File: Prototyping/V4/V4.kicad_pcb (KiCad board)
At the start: 2 copper layers, 126.7 x 100.2 mm, 117 parts, among them J1 Conn_02x04_Odd_Even, SW1 SW_Push_45deg, SW10 SW_Push_45deg, SW11 SW_Push_45deg, SW12 SW_Push_45deg, SW13 SW_Push_45deg, SW14 SW_Push_45deg, SW15 SW_Push_45deg, SW16 SW_Push_45deg, SW17 SW_Push_45deg, SW18 SW_Push_45deg, SW19 SW_Push_45deg, SW2 SW_Push_45deg, SW20 SW_Push_45deg, SW21 SW_Push_45deg, SW22 SW_Push_45deg, SW23 SW_Push_45deg, SW24 SW_Push_45deg, SW25 SW_Push_45deg, SW26 SW_Push_45deg, SW27 SW_Push_45deg, SW28 SW_Push_45deg, SW29 SW_Push_45deg, SW3 SW_Push_45deg, SW30 SW_Push_45deg, SW31 SW_Push_45deg, SW32 SW_Push_45deg, SW33 SW_Push_45deg, SW34 SW_Push_45deg, SW35 SW_Push_45deg, SW36 SW_Push_45deg, SW37 SW_Push_45deg, SW38 SW_Push_45deg, SW39 SW_Push_45deg, SW4 SW_Push_45deg, SW40 SW_Push_45deg, SW41 SW_Push_45deg, SW42 SW_Push_45deg, SW43 SW_Push_45deg, SW44 SW_Push_45deg, SW45 SW_Push_45deg, SW46 SW_Push_45deg, SW47 SW_Push_45deg, SW48 SW_Push_45deg, SW5 SW_Push_45deg, SW51 SW_Push_45deg, SW52 SW_Push_45deg, SW53 SW_Push_45deg, SW54 SW_Push_45deg, SW55 SW_Push_45deg, SW56 SW_Push_45deg, SW57 SW_Push_45deg, SW58 SW_Push_45deg, SW6 SW_Push_45deg, SW7 SW_Push_45deg, SW8 SW_Push_45deg, SW9 SW_Push_45deg

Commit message: validating
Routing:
- net Row 2: track 141.4 -> 144.8 mm
- net Row 1: track 121.1 -> 121.8 mm
- net C56: track 306.2 -> 306.8 mm

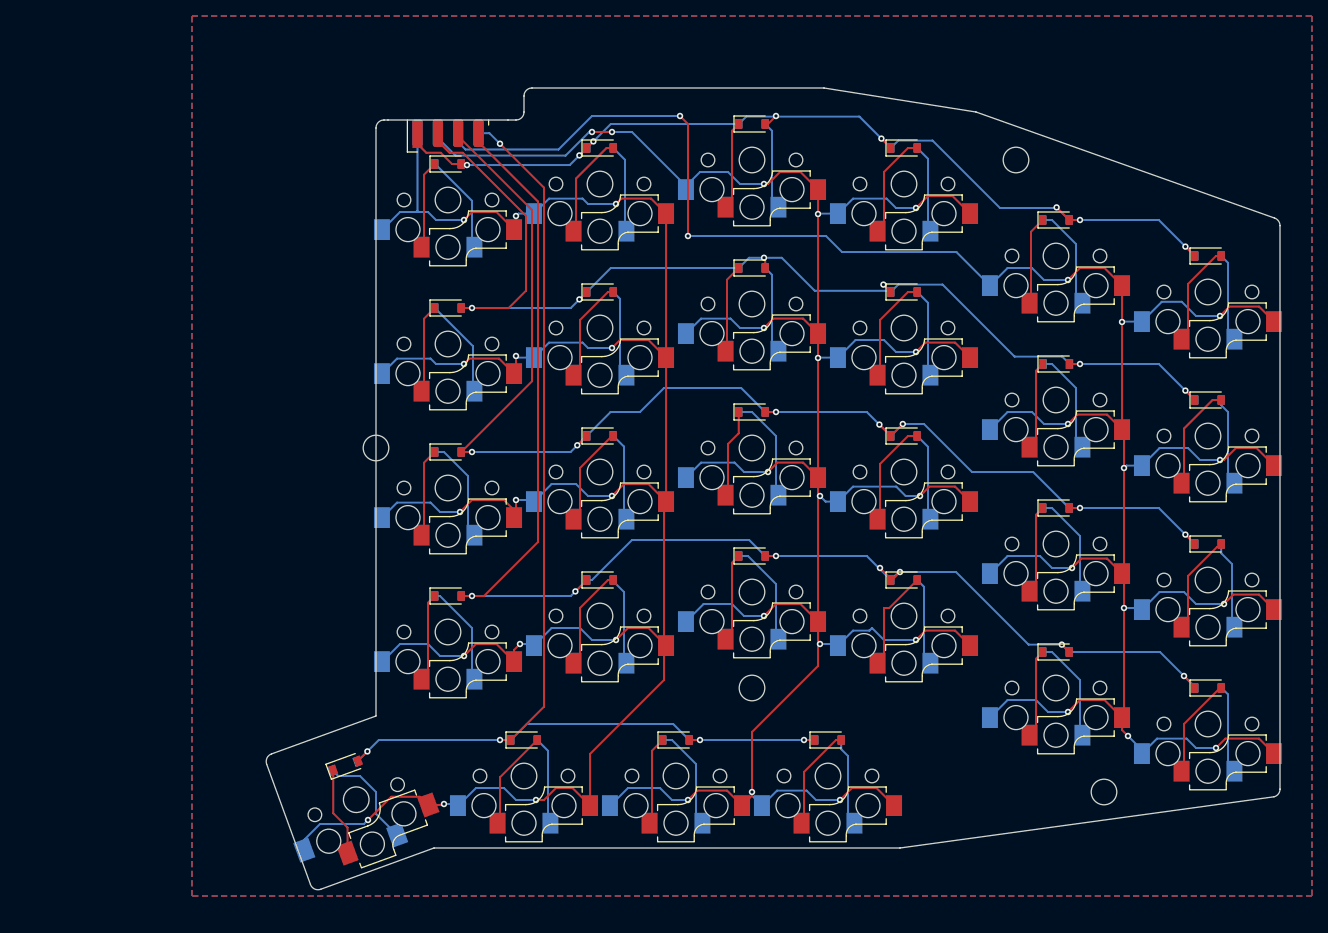
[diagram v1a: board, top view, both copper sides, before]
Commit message: fix diode direction, missing wire, and pin position
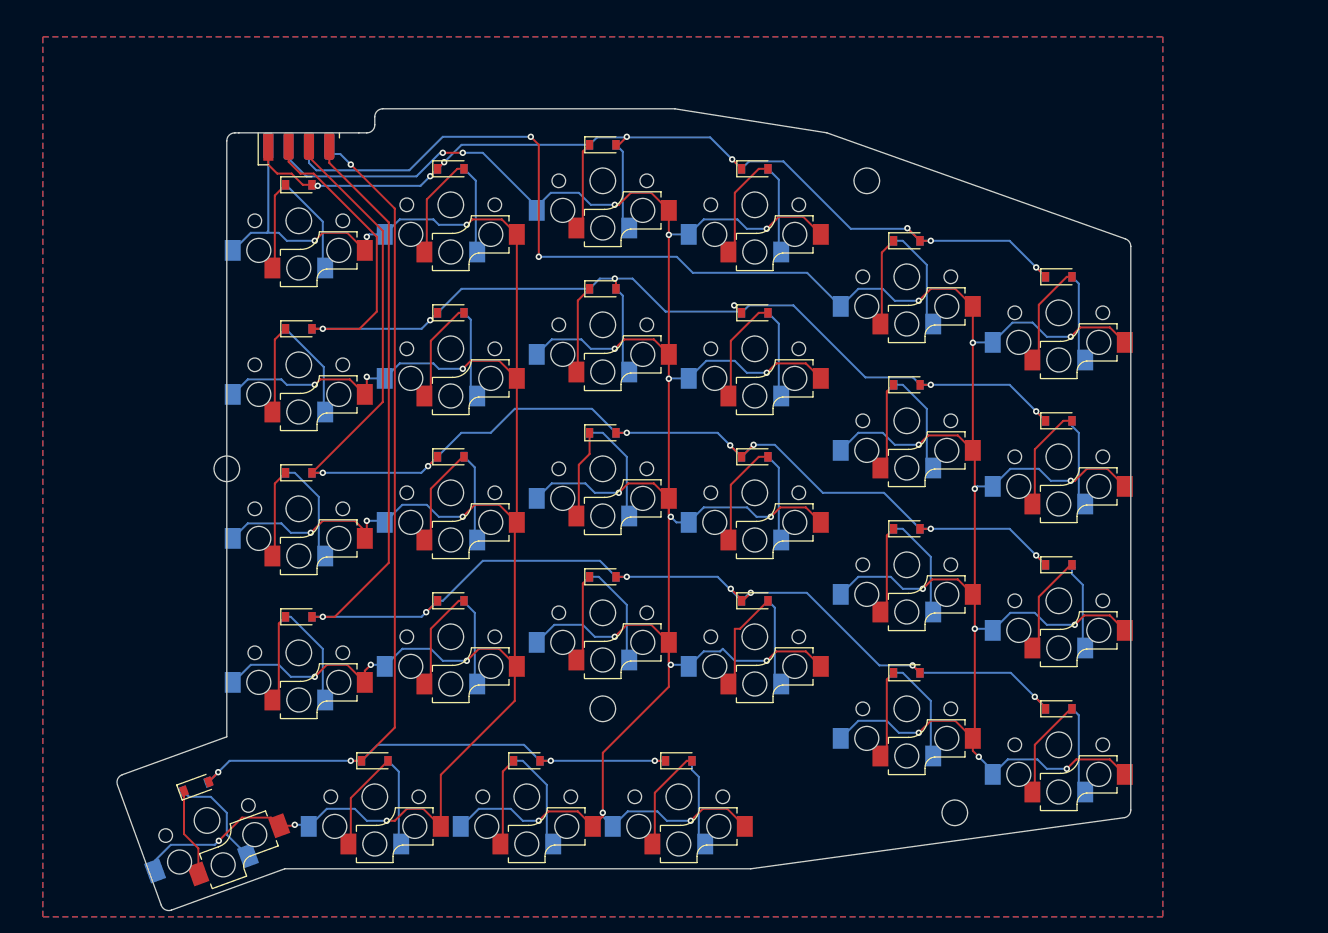
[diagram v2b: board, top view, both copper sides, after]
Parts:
- moved D10 18.8 mm to (190.3, 59.1)
- moved D3 18.8 mm to (190.3, 59.1)
- moved D32 18.8 mm to (152.3, 95.1)
- moved D4 18.8 mm to (171.3, 56.1)
- moved D5 18.8 mm to (152.3, 59.1)
- moved D6 18.8 mm to (133.3, 61.1)
- moved D7 18.8 mm to (133.3, 61.1)
- moved D8 18.8 mm to (152.3, 59.1)
- moved D9 18.8 mm to (171.3, 56.1), turned to 0 degrees
- moved H3 18.8 mm to (204.3, 60.6)
- moved SW10 18.8 mm to (190.3, 63.6)
- moved SW3 18.8 mm to (190.3, 63.6)
- moved SW4 18.8 mm to (171.3, 60.6)
- moved SW5 18.8 mm to (152.3, 63.6)
- moved SW8 18.8 mm to (152.3, 63.6)
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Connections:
- D21 pad 1: Net-(D21-Pad1) -> Row 2
- D21 pad 2: Row 2 -> Net-(D21-Pad2)
- D9 pad 1: Net-(D9-Pad1) -> Row 1
- D9 pad 2: Row 1 -> Net-(SW9-Pad2)
- SW21 pad 2: Net-(D21-Pad1) -> Net-(D21-Pad2)
- SW9 pad 2: Net-(D9-Pad1) -> Net-(SW9-Pad2)
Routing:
- net Net-(SW9-Pad2): track 0.00 -> 9.95 mm
- net Net-(D9-Pad1): track 9.95 -> 0.00 mm
- net Net-(D21-Pad1): track 9.95 -> 0.00 mm
- net Net-(D21-Pad2): track 0.00 -> 9.95 mm
- net Row 2: track 144.8 -> 146.2 mm
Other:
- outline, holes or cut-outs redrawn

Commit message: add descriptive text
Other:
- board text added: "Left"
- board text added: "Pragmatic 56 Duplex Matrix R1"
- board text added: "Right"
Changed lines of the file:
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@@
   (gr_line (start 237.35 139.242893) (end 237.35 68.807107) (layer "Edge.Cuts") (width 0.1))
   (gr_line (start 125.85 54.61) (end 125.35 54.61) (layer "Edge.Cuts") (width 0.1))
+  (gr_text "Right\n" (at 142.875 61.1) (layer "B.SilkS")
+    (effects (font (size 1.5 1.5) (thickness 0.2)) (justify mirror))
+  )
+  (gr_text "Pragmatic 56\nDuplex Matrix\nR1" (at 201.295 139.7) (layer "F.SilkS")
+    (effects (font (size 1.5 1.5) (thickness 0.2)))
+  )
+  (gr_text "Left" (at 142.875 61.1) (layer "F.SilkS")
+    (effects (font (size 1.5 1.5) (thickness 0.2)))
+  )
   (dimension (type aligned) (layer "Cmts.User")
     (pts (xy 125.85 55.6) (xy 140.85 55.6))

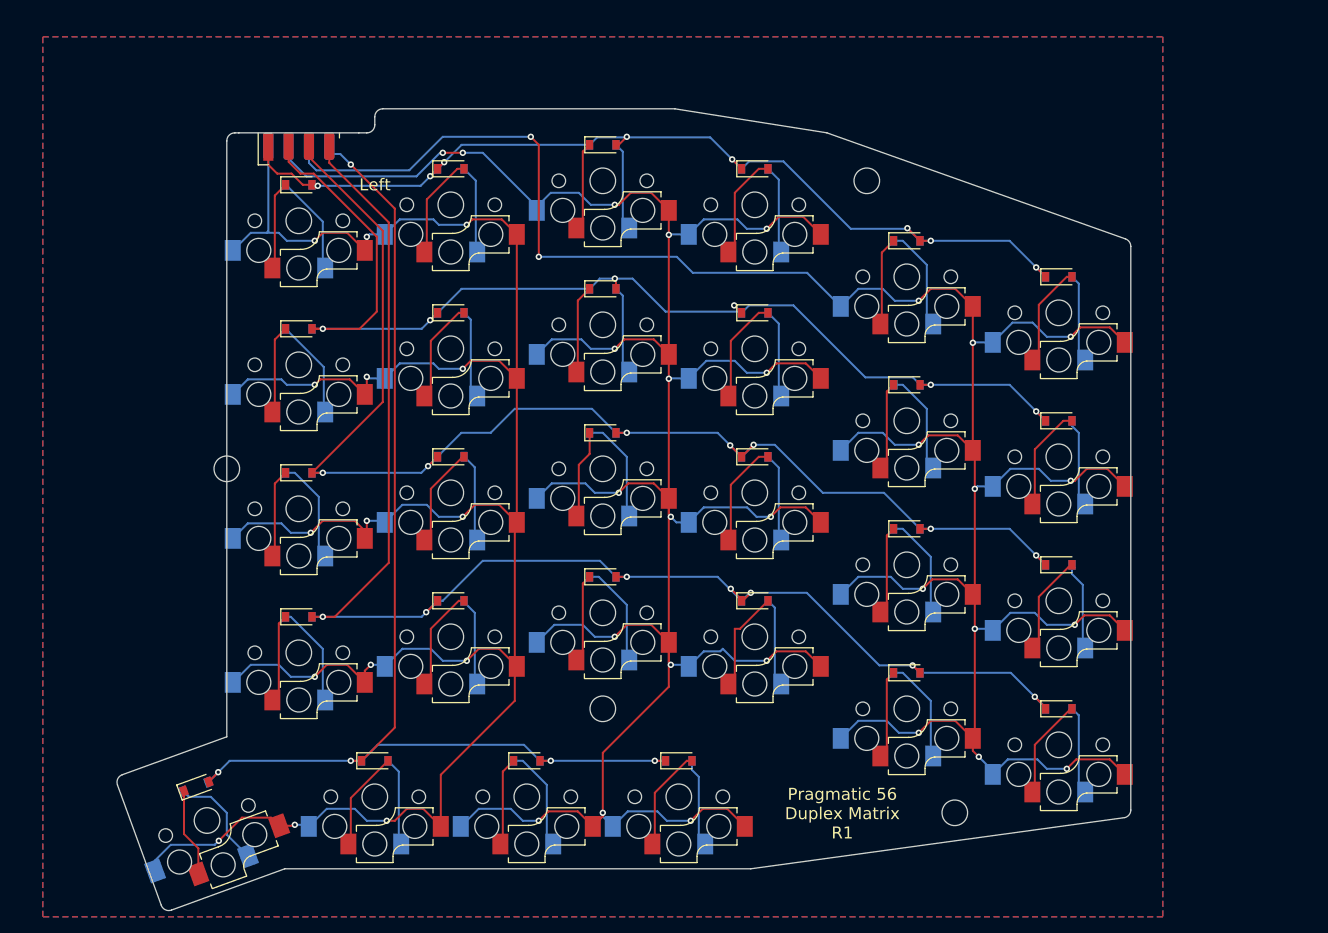
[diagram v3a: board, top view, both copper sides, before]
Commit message: fix footprint
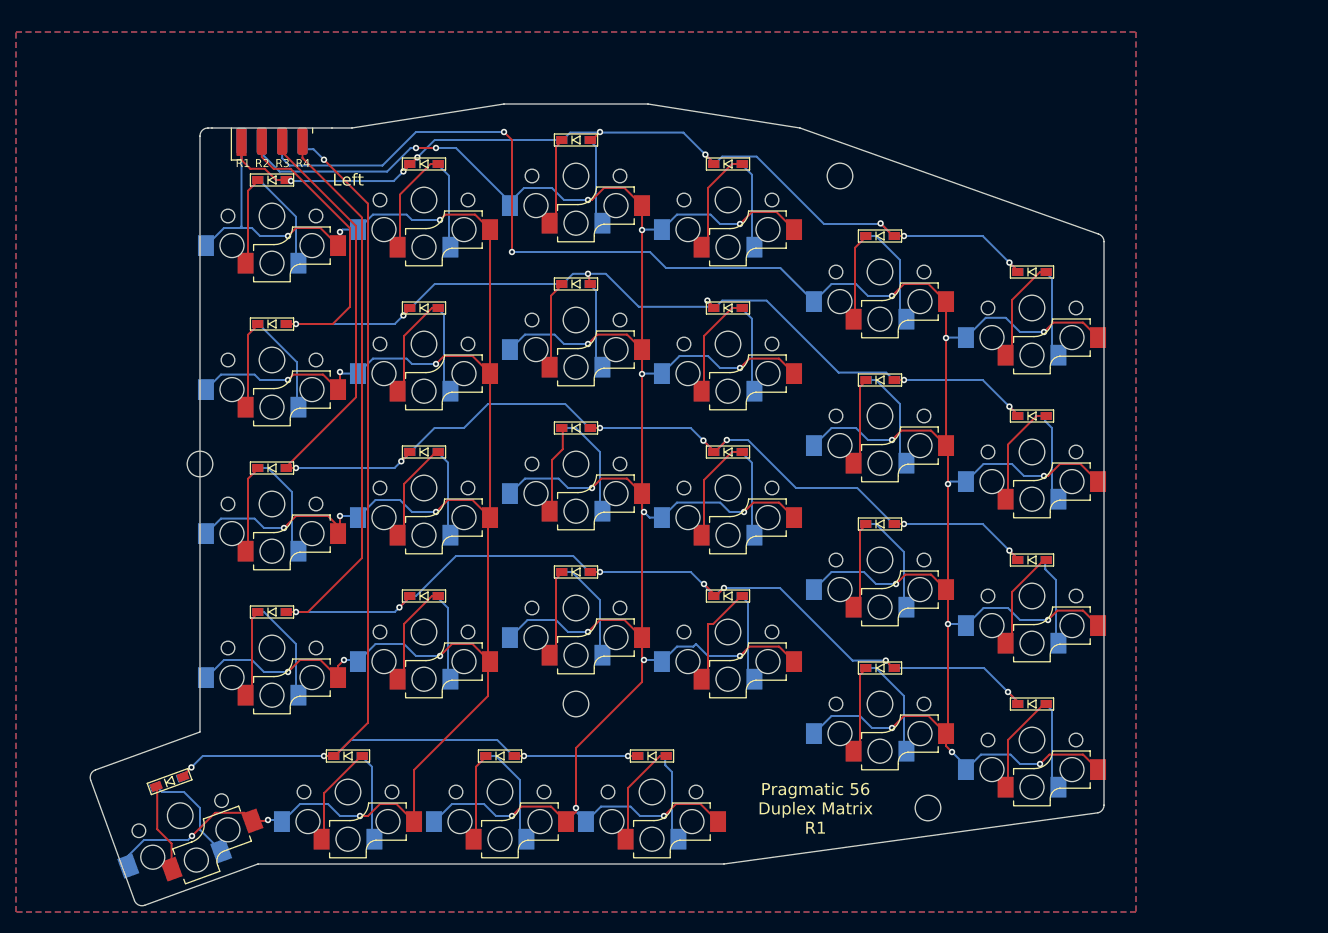
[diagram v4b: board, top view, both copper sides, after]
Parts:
- D1, D10, D11, D12, D13, D14, D15, D16, D17, D18, D19, D2, D20, D21, D22, D23, D24, D25, D26, D27, D28, D29, D3, D30, D31, D32, D33, D34, D35, D36, D37, D38, D39, D4, D40, D41, D42, D43, D44, D45, D46, D47, D48, D5, D51, D52, D53, D54, D55, D56, D57, D58, D6, D7, D8, D9: footprint Diode_SMD:D_SOD-123 -> Keyboard_Foostan:D3_SMD_v2
- moved J1 3.41 mm to (130.0, 54.0)
- moved D54 3.40 mm to (117.2, 135.7)
- moved D32 3.40 mm to (149.0, 94.5)
- moved D10 3.40 mm to (187.0, 58.5)
- moved D3 3.40 mm to (187.0, 58.5)
- moved D4 3.40 mm to (168.0, 55.5)
- moved D5 3.40 mm to (149.0, 58.5)
- moved D6 3.40 mm to (130.0, 60.5)
- moved D7 3.40 mm to (130.0, 60.5)
- moved D8 3.40 mm to (149.0, 58.5)
- moved D9 3.40 mm to (168.0, 55.5)
- moved H3 3.40 mm to (201.0, 60.0)
- moved SW10 3.40 mm to (187.0, 63.0)
- moved SW3 3.40 mm to (187.0, 63.0)
- moved SW4 3.40 mm to (168.0, 60.0)
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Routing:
- net Row 1: track 121.8 -> 120.3 mm
- net Row 2: track 146.2 -> 144.8 mm
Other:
- outline, holes or cut-outs redrawn
- board text added: "C1"
- board text added: "C3"
- board text added: "C5"
- board text added: "R1"
- board text added: "R2"
- board text added: "R3"
- board text added: "R4"
- board text added: "R5"

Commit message: decals
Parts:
- added REF**: OSHW-Logo2_7.3x6mm_Copper, Keyboard_JSA:OSHW-Logo2_7.3x6mm_Copper, B.Cu at (194.0, 138.0)
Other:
- board text added: "Pragmatic 56 Duplex Matrix R1 2023-02"
- board text removed: "Pragmatic 56 Duplex Matrix R1"
